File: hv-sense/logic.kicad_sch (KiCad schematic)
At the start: 33 parts, among them U1 4081, U2 4071, U3 4081, U4 40106, U5 40106, U6 4013

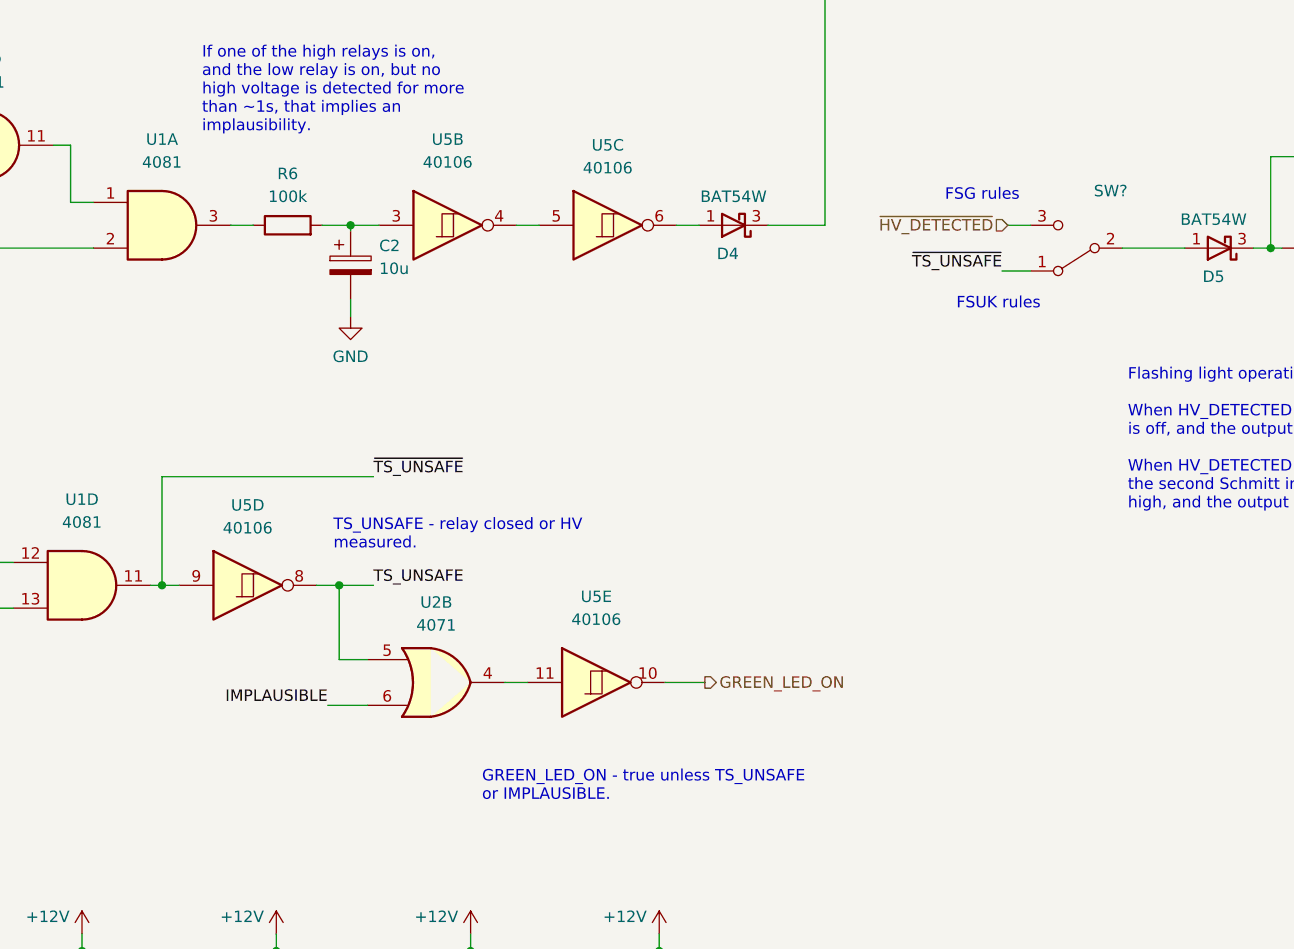
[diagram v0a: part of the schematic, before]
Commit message: feat(hvs): update to actual latest existing designs
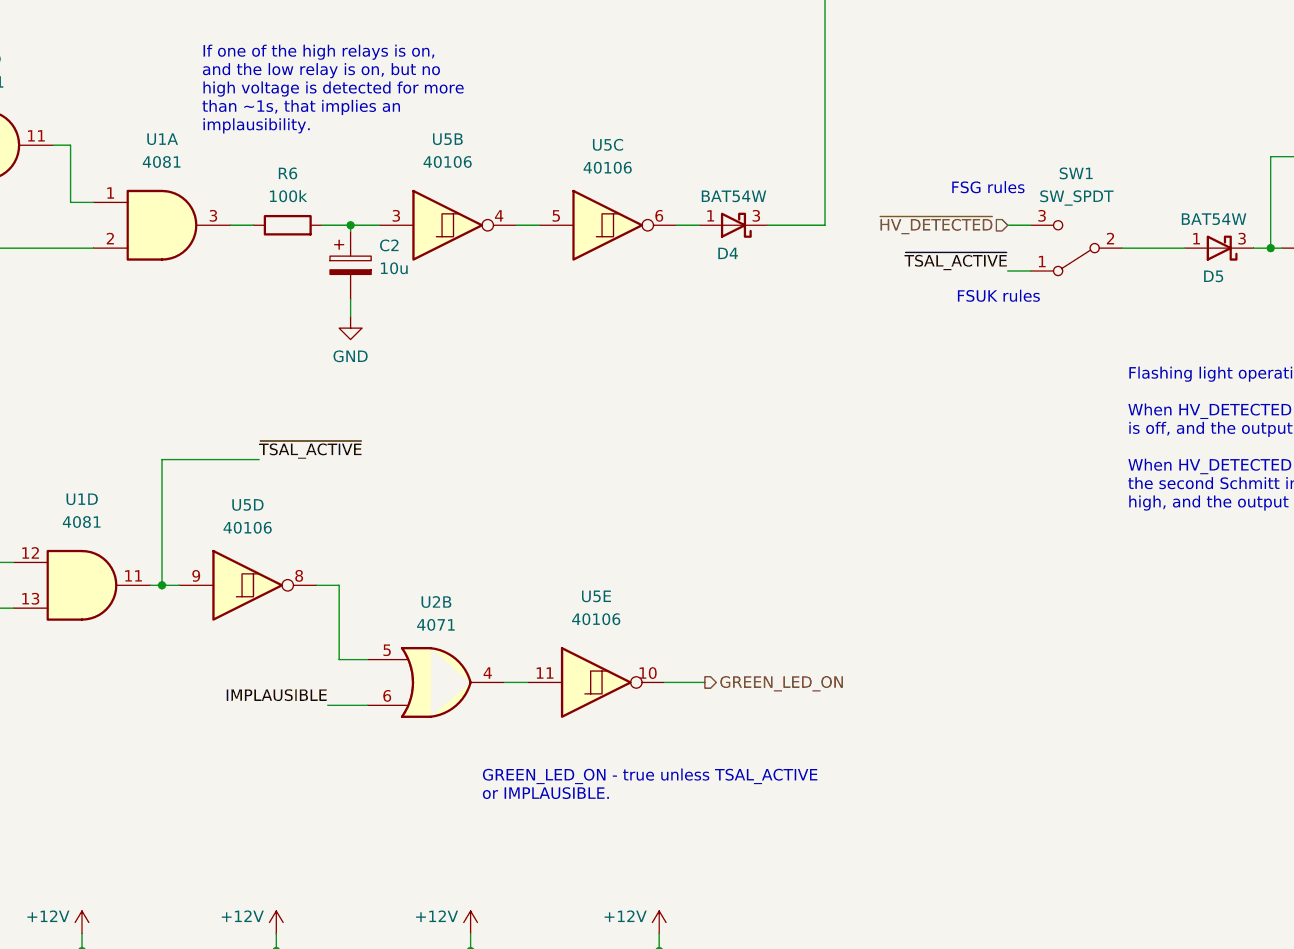
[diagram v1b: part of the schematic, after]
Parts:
- removed SW?: (no value), symbol Switch:SW_SPDT
- added SW1: SW_SPDT, Connector_PinHeader_2.54mm:PinHeader_1x03_P2.54mm_Vertical, symbol Switch:SW_SPDT
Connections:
- net ~{HV_DETECTED}: now also SW1.3 (C)
- net at D5.1 (A): now also SW1.2 (B)
- net TS_UNSAFE: no longer names the net of U2.5, U5.8
- net ~{TS_UNSAFE} renamed ~{TSAL_ACTIVE}
- net ~{TSAL_ACTIVE}: now also SW1.1 (A)
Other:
- note added: "GREEN_LED_ON - true unless TSAL_ACTIVE or IMPLAUSIBLE."
- note removed: "GREEN_LED_ON - true unless TS_UNSAFE or IMPLAUSIBLE."
- note removed: "TS_UNSAFE - relay closed or HV measured."
- company: (none) -> SUFST - Southampton University Formula Student Team
- title: (none) -> TSAL Sense / Logic - Implausibility Check

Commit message: feat(hvs): add fusing to HV input
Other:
- company: SUFST - Southampton University Formula Student Team -> SUFST 
- title: TSAL Sense / Logic - Implausibility Check -> HV Sense
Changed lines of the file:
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@@
 (kicad_sch (version 20211123) (generator eeschema)
-  (paper "A3")
+  (paper "A4")
   (title_block
-    (title "TSAL Sense / Logic - Implausibility Check")
+    (title "HV Sense")
     (date "2022-04-01")
-    (rev "1")
-    (company "SUFST - Southampton University Formula Student Team")
+    (rev "1.0.1")
+    (company "SUFST ")
+    (comment 1 "STAG 9")
+    (comment 3 "Marek Frodyma")
   )
   (junction (at 116.205 79.375) (diameter 0) (color 0 0 0 0)

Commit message: feat(hvs): downsize precharge relay contact wetting resistor
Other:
- company: SUFST  -> SUFST - Southampton University Formula Student Team
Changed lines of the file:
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@@
   (title_block
     (title "HV Sense")
-    (date "2022-04-01")
-    (rev "1.0.1")
-    (company "SUFST ")
+    (date "2023-04-02")
+    (rev "1.1.0")
+    (company "SUFST - Southampton University Formula Student Team")
     (comment 1 "STAG 9")
     (comment 3 "Marek Frodyma")
